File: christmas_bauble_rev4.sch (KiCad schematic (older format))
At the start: 23 parts

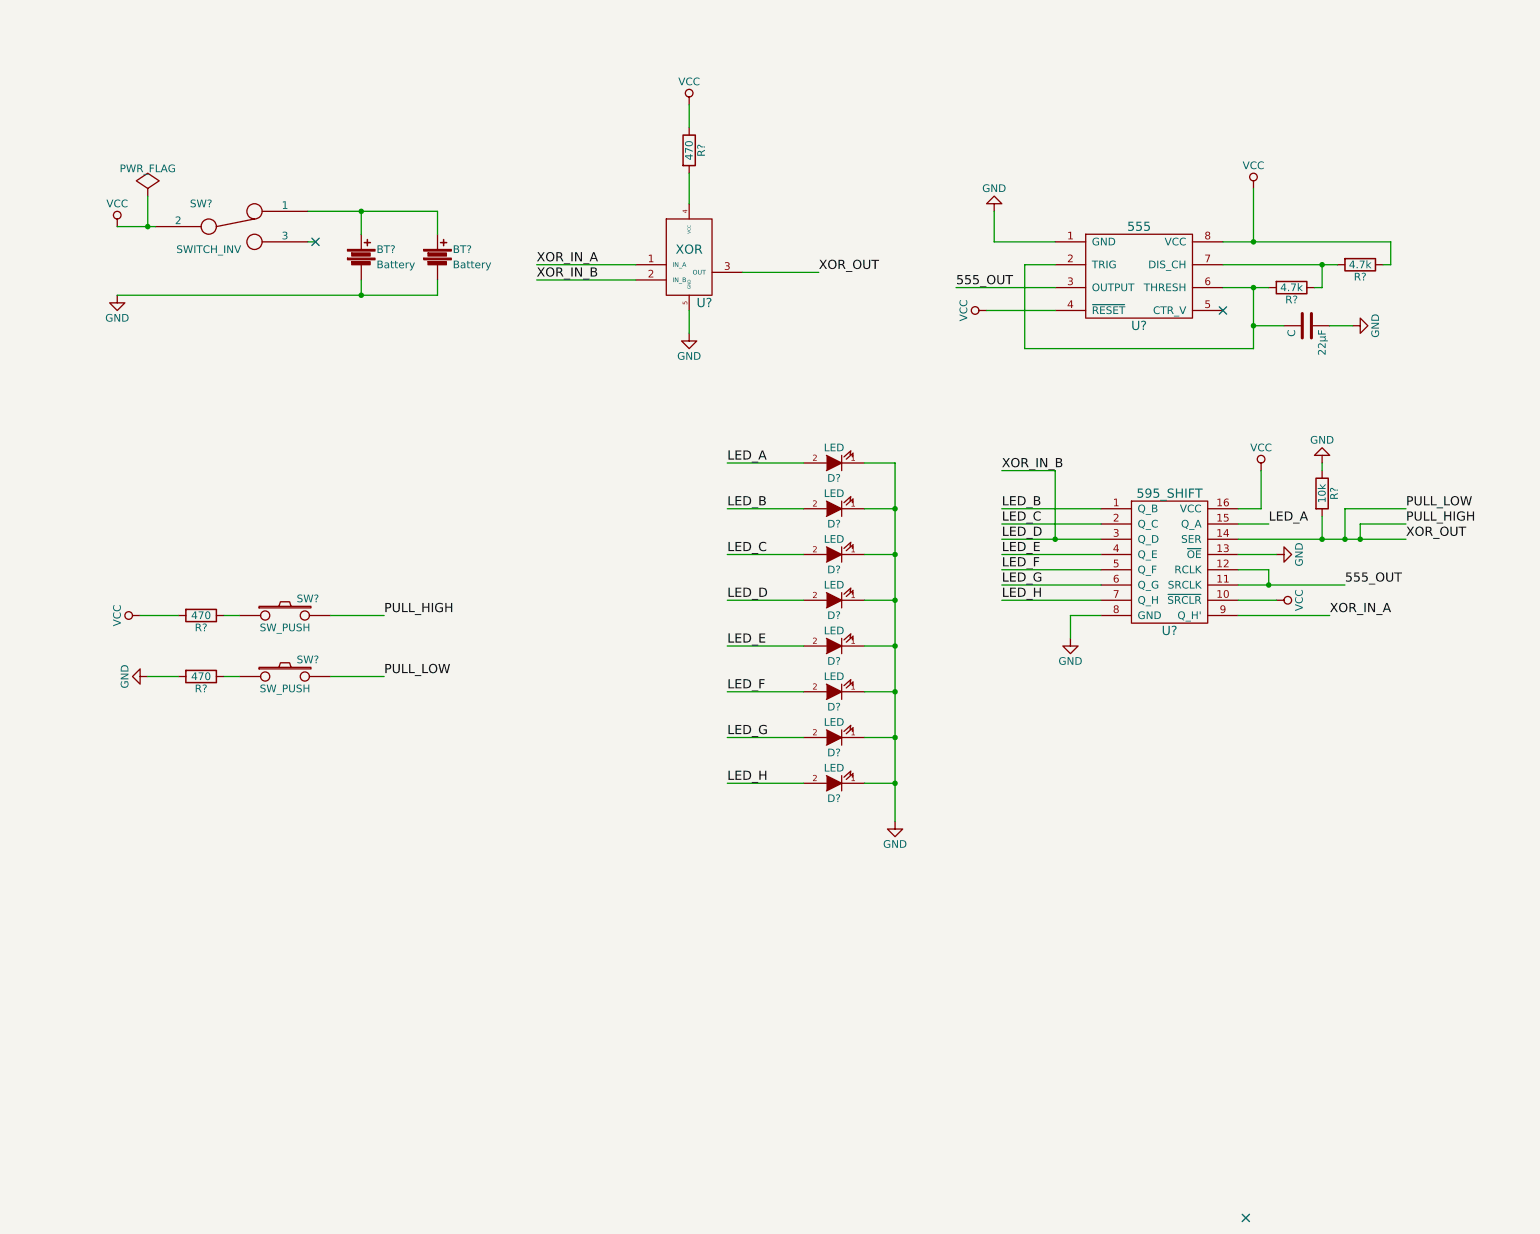
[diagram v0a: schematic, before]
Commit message: Adding dip switches to the layout to program the bauble
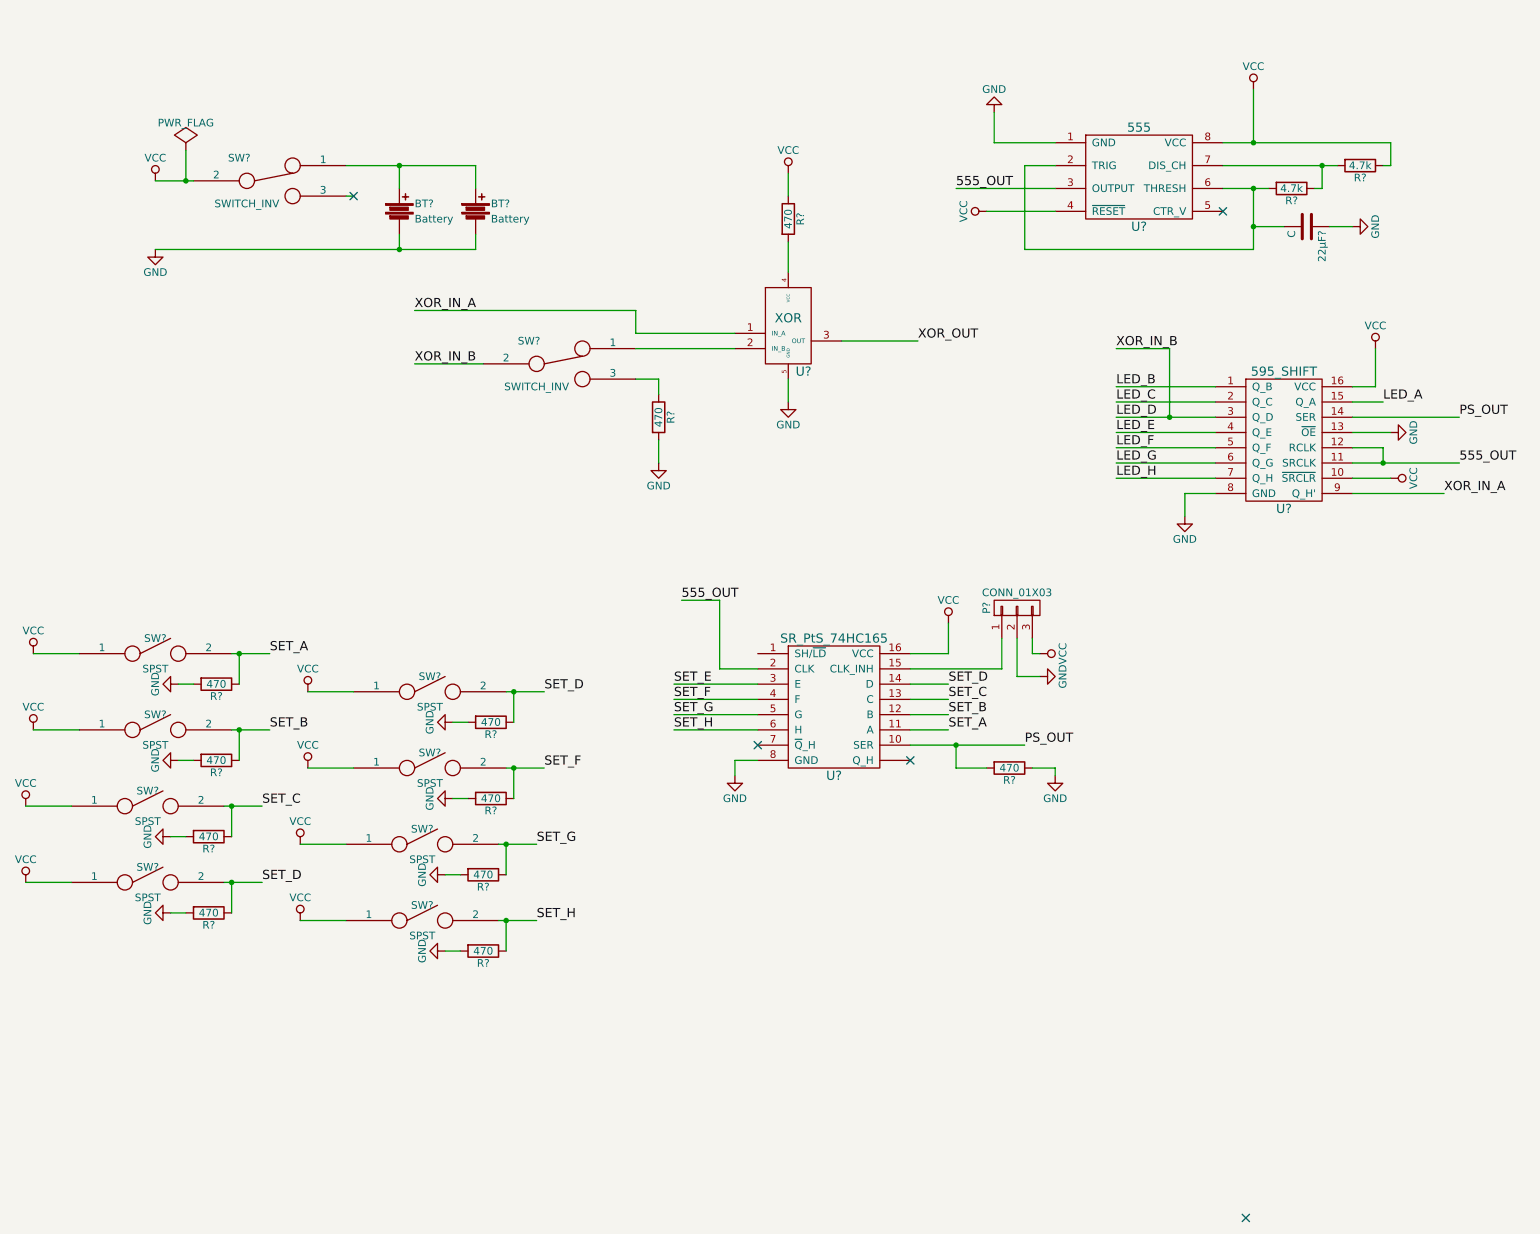
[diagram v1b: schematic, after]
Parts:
- removed D? (x8): LED, symbol LED
- removed R?: 10k, symbol R
- removed R? (x2): 470, symbol R
- removed SW? (x2): SW_PUSH, symbol SW_PUSH
- added P?: CONN_01X03, symbol CONN_01X03
- added R? (x10): 470, symbol R
- added SW? (x8): SPST, symbol SPST
- added SW?: SWITCH_INV, symbol SWITCH_INV
- added U?: SR_PtS_74HC165, symbol SR_PtS_74HC165
- renumbered 22µF to 22µF?
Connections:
- net 555_OUT: now also U?.2 (CLK)
- net GND: now also P?.2 (P2), R?.1, R?.2, R?.2, R?.2, R?.2, R?.2, R?.2, R?.2, R?.2, R?.2, U?.8 (GND)
- net LED_D: now also SW?.2; no longer U?.2 (IN_B)
- net VCC: now also P?.3 (P3), SW?.1, SW?.1, SW?.1, SW?.1, SW?.1, SW?.1, SW?.1, SW?.1, U?.16 (VCC)
- net PULL_HIGH renamed PS_OUT
- net PS_OUT: now also R?.2, U?.10 (SER); no longer U?.3 (OUT)
- new net: SW?.1, U?.2 (IN_B)
- new net: P?.1 (P1), U?.15 (CLK_INH)
- new net: R?.1, SW?.3
- new net SET_A: R?.1, SW?.2, U?.11 (A)
- new net SET_B: R?.1, SW?.2, U?.12 (B)
- new net SET_C: R?.1, SW?.2, U?.13 (C)
- new net SET_D: R?.1, R?.1, SW?.2, SW?.2, U?.14 (D)
- new net SET_E: U?.3 (E)
- new net SET_F: R?.1, SW?.2, U?.4 (F)
- new net SET_G: R?.1, SW?.2, U?.5 (G)
- new net SET_H: R?.1, SW?.2, U?.6 (H)
- new net XOR_OUT: U?.3 (OUT)
- no-connect marks 3 -> 5
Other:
- moved on the sheet: 22µF?, BT?, R?, SW?, U?

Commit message: Adding more debugging LEDs and a switch for 'Programmer mode'
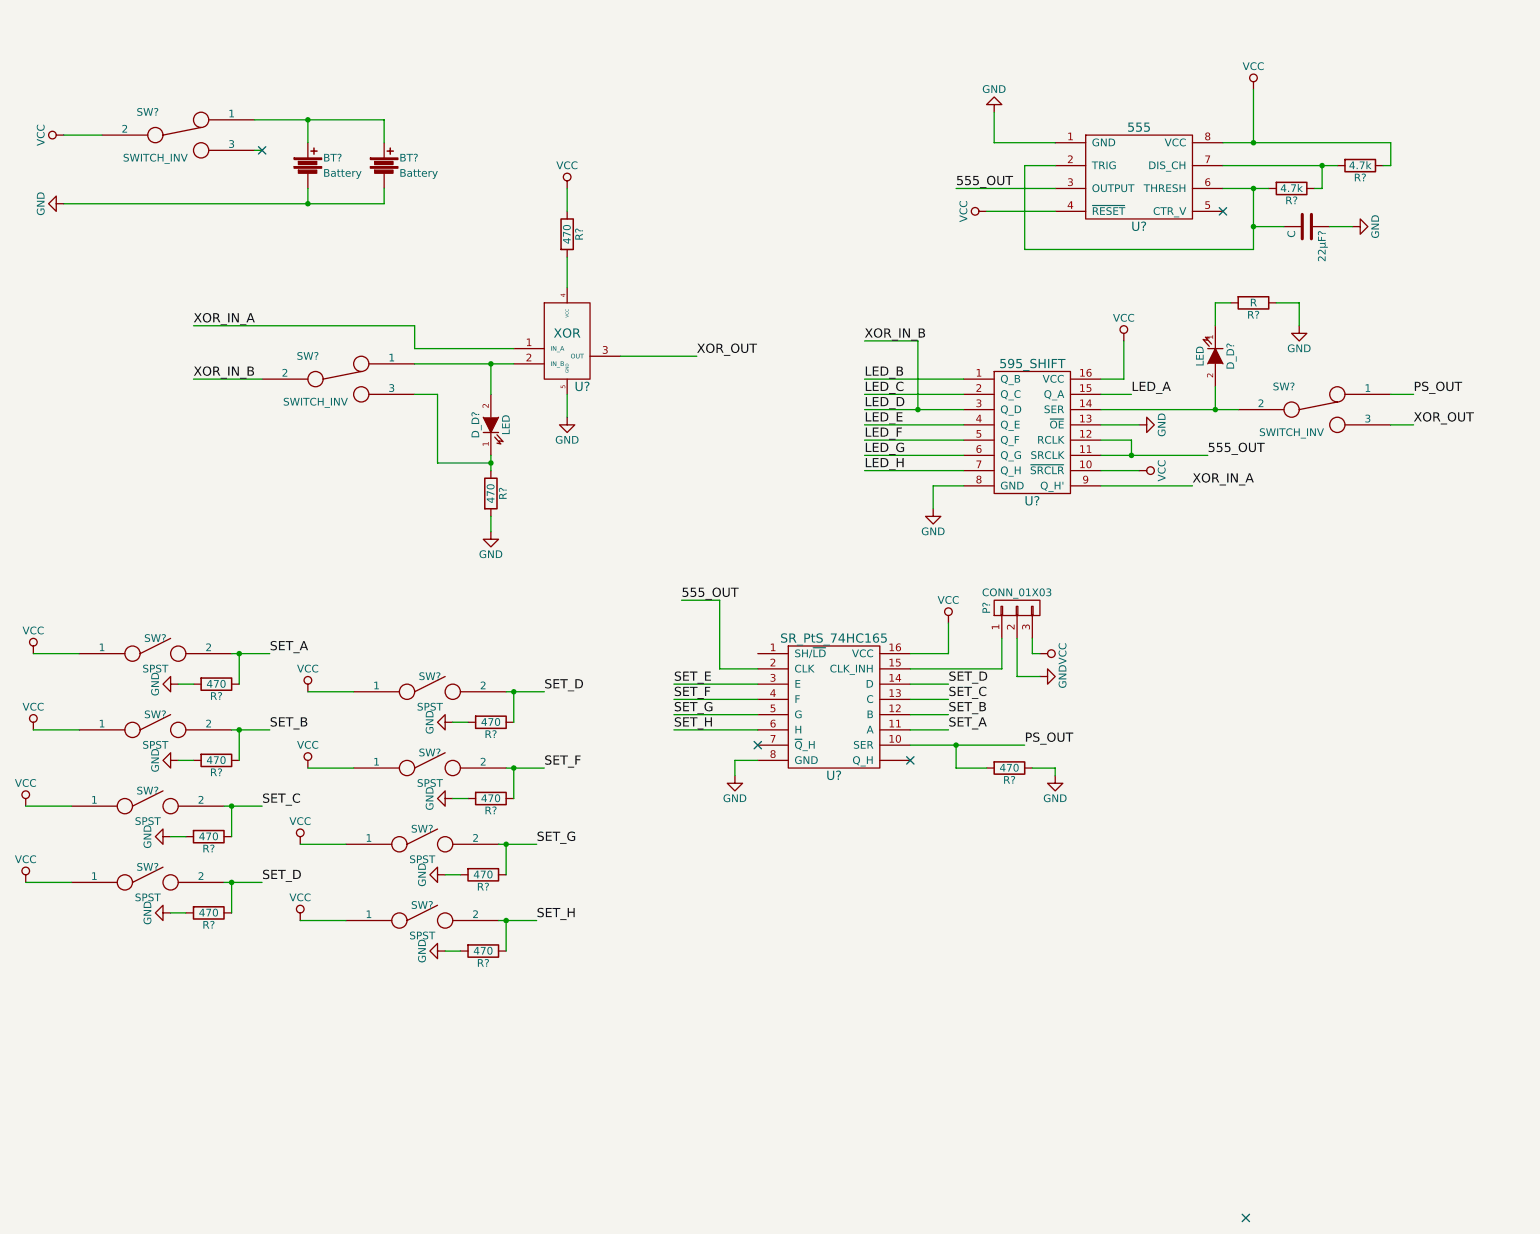
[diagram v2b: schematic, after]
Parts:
- removed R?: 470, symbol R
- added D_D? (x2): LED, symbol LED
- added R?: 470, symbol R
- added R?: R, symbol R
- added SW?: SWITCH_INV, symbol SWITCH_INV
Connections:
- net GND: now also R?.1, R?.2
- net PS_OUT: now also SW?.1; no longer U?.14 (SER)
- net XOR_OUT: now also SW?.3
- net at SW?.1, U?.2 (IN_B): now also D_D?.2 (A)
- net at SW?.3: now also D_D?.1 (K), R?.1
- new net: D_D?.2 (A), SW?.2, U?.14 (SER)
- new net: D_D?.1 (K), R?.2
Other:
- moved on the sheet: BT?, R?, SW?, U?

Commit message: Updating some revision 4 files.
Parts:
- removed D_D? (x2): LED, symbol LED
- removed R?: 4.7k, symbol R
- removed R? (x2): 470, symbol R
- removed R?: R, symbol R
- added D?: D, symbol D
- added P? (x2): CONN_01X03, symbol CONN_01X03
- added VR?: VR, symbol VR
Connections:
- net GND: now also P?.1 (P1), P?.3 (P3)
- net PS_OUT: now also U?.~ (Q_H); no longer U?.10 (SER)
- net VCC: now also P?.1 (P1), P?.3 (P3), VR?.1
- net at 22µF?.2, R?.2, U?.2 (TRIG)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: now also D?.1 (K)
- net at R?.1, U?.7 (DIS_CH): now also D?.2 (A), VR?.2
- net at U?.1 (SH/~LD): now also P?.2 (P2)
- new net: P?.2 (P2), U?.10 (SER)
- no-connect marks 5 -> 7
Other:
- note added: "Test Freq"
- moved on the sheet: 22µF?
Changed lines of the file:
@@
 Sheet 1 1
 Title "Christmas Bauble"
-Date "2016-01-01"
-Rev "Rev 4"
+Date "2016-02-13"
+Rev "Rev B"
 Comp ""
 Comment1 "Revision that gets put into production for soldering kits"
@@
 $EndComp
 $Comp
-L R R?
-U 1 1 5685F423
-P 9450 1500
-F 0 "R?" V 9530 1500 50  0000 C CNN
-F 1 "4.7k" V 9450 1500 50  0000 C CNN
-F 2 "" V 9380 1500 30  0000 C CNN
-F 3 "" H 9450 1500 30  0000 C CNN
-	1    9450 1500
-	0    1    1    0
-$EndComp
-$Comp
 L VCC #PWR?
 U 1 1 5685F6A7
@@
 L C 22µF?
 U 1 1 56860DDF
-P 9100 1900
-F 0 "22µF?" H 9125 2000 50  0000 L CNN
-F 1 "C" H 9125 1800 50  0000 L CNN
-F 2 "" H 9138 1750 30  0000 C CNN
-F 3 "" H 9100 1900 60  0000 C CNN
-	1    9100 1900
+P 9100 2350
+F 0 "22µF?" H 9125 2450 50  0000 L CNN
+F 1 "C" H 9125 2250 50  0000 L CNN
+F 2 "" H 9138 2200 30  0000 C CNN
+F 3 "" H 9100 2350 60  0000 C CNN
+	1    9100 2350
 	0    1    1    0
 $EndComp
@@
 L GND #PWR?
 U 1 1 56860ED4
-P 9400 1900
-F 0 "#PWR?" H 9400 1650 50  0001 C CNN
-F 1 "GND" H 9400 1750 50  0000 C CNN
-F 2 "" H 9400 1900 60  0000 C CNN
-F 3 "" H 9400 1900 60  0000 C CNN
-	1    9400 1900
+P 9400 2350
+F 0 "#PWR?" H 9400 2100 50  0001 C CNN
+F 1 "GND" H 9400 2200 50  0000 C CNN
+F 2 "" H 9400 2350 60  0000 C CNN
+F 3 "" H 9400 2350 60  0000 C CNN
+	1    9400 2350
 	0    -1   -1   0
 $EndComp
@@
 	1    0    0    -1
 $EndComp
-Text Label 5000 4350 0    60   ~ 0
+Text Label 4550 4350 0    60   ~ 0
 555_OUT
-Text Label 7250 5300 0    60   ~ 0
+Text Label 6750 5400 0    60   ~ 0
 PS_OUT
-NoConn ~ 6500 5400
 NoConn ~ 5500 5300
 $Comp
@@
 PS_OUT
 $Comp
-L R R?
-U 1 1 568DB16E
-P 7150 5450
-F 0 "R?" V 7230 5450 50  0000 C CNN
-F 1 "470" V 7150 5450 50  0000 C CNN
-F 2 "" V 7080 5450 30  0000 C CNN
-F 3 "" H 7150 5450 30  0000 C CNN
-	1    7150 5450
-	0    1    1    0
-$EndComp
-$Comp
 L GND #PWR?
 U 1 1 568DB280
-P 7450 5500
-F 0 "#PWR?" H 7450 5250 50  0001 C CNN
-F 1 "GND" H 7450 5350 50  0000 C CNN
-F 2 "" H 7450 5500 60  0000 C CNN
-F 3 "" H 7450 5500 60  0000 C CNN
-	1    7450 5500
+P 7850 5350
+F 0 "#PWR?" H 7850 5100 50  0001 C CNN
+F 1 "GND" H 7850 5200 50  0000 C CNN
+F 2 "" H 7850 5350 60  0000 C CNN
+F 3 "" H 7850 5350 60  0000 C CNN
+	1    7850 5350
 	1    0    0    -1
 $EndComp
@@
 $EndComp
 $Comp
-L LED D_D?
-U 1 1 568DC6DF
-P 3750 3200
-F 0 "D_D?" H 3750 3300 50  0000 C CNN
-F 1 "LED" H 3750 3100 50  0000 C CNN
-F 2 "" H 3750 3200 60  0000 C CNN
-F 3 "" H 3750 3200 60  0000 C CNN
-	1    3750 3200
-	0    -1   -1   0
-$EndComp
-$Comp
-L R R?
-U 1 1 568DC944
-P 3750 3650
-F 0 "R?" V 3830 3650 50  0000 C CNN
-F 1 "470" V 3750 3650 50  0000 C CNN
-F 2 "" V 3680 3650 30  0000 C CNN
-F 3 "" H 3750 3650 30  0000 C CNN
-	1    3750 3650
-	1    0    0    -1
-$EndComp
-$Comp
-L GND #PWR?
-U 1 1 568DCA56
-P 3750 3900
-F 0 "#PWR?" H 3750 3650 50  0001 C CNN
-F 1 "GND" H 3750 3750 50  0000 C CNN
-F 2 "" H 3750 3900 60  0000 C CNN
-F 3 "" H 3750 3900 60  0000 C CNN
-	1    3750 3900
-	1    0    0    -1
-$EndComp
-$Comp
 L SWITCH_INV SW?
 U 1 1 568DD1E4
@@
 Connection ~ 6550 3100
 Wire Wire Line
-	8750 1650 8750 2050
-Wire Wire Line
-	8750 2050 7250 2050
-Wire Wire Line
-	7250 2050 7250 1500
+	8750 1650 8750 2350
+Wire Wire Line
+	7250 2000 8850 2000
+Wire Wire Line
+	7250 2000 7250 1500
 Wire Wire Line
 	7250 1500 7450 1500
@@
 	8550 1650 8850 1650
 Wire Wire Line
-	8550 1500 9300 1500
+	8550 1500 9400 1500
 Wire Wire Line
 	9150 1650 9200 1650
 Wire Wire Line
-	9200 1650 9200 1500
+	9200 1500 9200 2000
 Connection ~ 9200 1500
 Wire Wire Line
-	9600 1500 9650 1500
-Wire Wire Line
-	9650 1500 9650 1350
-Wire Wire Line
-	9650 1350 8550 1350
+	9950 1350 9950 1500
+Wire Wire Line
+	8550 1350 9950 1350
 Wire Wire Line
 	8750 1350 8750 1000
@@
 	7450 1800 7000 1800
 Wire Wire Line
-	7450 1650 6800 1650
-Wire Wire Line
-	8750 1900 8950 1900
-Connection ~ 8750 1900
-Wire Wire Line
-	9250 1900 9400 1900
+	6800 1650 7450 1650
+Wire Wire Line
+	9250 2350 9400 2350
 Wire Wire Line
 	3900 2700 3250 2700
@@
 	5350 5400 5350 5500
 Wire Wire Line
-	5250 4350 5250 4800
-Wire Wire Line
-	5250 4800 5500 4800
-Wire Wire Line
-	5250 4350 5000 4350
-Wire Wire Line
-	6500 5300 7250 5300
+	4950 4800 5500 4800
+Wire Wire Line
+	4550 4350 4950 4350
 Wire Wire Line
 	1800 2900 2250 2900
@@
 	3250 3000 3400 3000
 Wire Wire Line
-	3400 3000 3400 3450
-Wire Wire Line
 	1800 2550 3250 2550
 Wire Wire Line
 	3250 2550 3250 2700
 Wire Wire Line
-	6800 5300 6800 5450
-Wire Wire Line
-	6800 5450 7000 5450
-Connection ~ 6800 5300
-Wire Wire Line
-	7300 5450 7450 5450
-Wire Wire Line
-	7450 5450 7450 5500
+	7500 5300 7850 5300
+Wire Wire Line
+	7850 5300 7850 5350
 Wire Wire Line
 	6500 4800 7100 4800
@@
 Connection ~ 3750 2800
 Wire Wire Line
-	3750 3400 3750 3500
-Wire Wire Line
-	3750 3800 3750 3900
-Wire Wire Line
-	3400 3450 3750 3450
-Connection ~ 3750 3450
-Wire Wire Line
 	9800 3000 9650 3000
 Wire Wire Line
@@
 Wire Wire Line
 	7750 3100 8650 3100
-$Comp
-L LED D_D?
-U 1 1 568DE83B
-P 8500 2750
-F 0 "D_D?" H 8500 2850 50  0000 C CNN
-F 1 "LED" H 8500 2650 50  0000 C CNN
-F 2 "" H 8500 2750 60  0000 C CNN
-F 3 "" H 8500 2750 60  0000 C CNN
-	1    8500 2750
-	0    1    1    0
-$EndComp
-Wire Wire Line
-	8500 2950 8500 3100
+Wire Wire Line
+	7350 1650 7350 650
+Wire Wire Line
+	7350 650  7950 650
+Connection ~ 7350 1650
+Text Notes 7850 600  0    60   ~ 0
+Test Freq
+$Comp
+L VR VR?
+U 1 1 568D51BE
+P 9650 1500
+F 0 "VR?" V 9710 1454 50  0000 C TNN
+F 1 "VR" V 9650 1500 50  0000 C CNN
+F 2 "" H 9650 1500 60  0000 C CNN
+F 3 "" H 9650 1500 60  0000 C CNN
+	1    9650 1500
+	0    1    1    0
+$EndComp
+Wire Wire Line
+	9950 1500 9900 1500
+NoConn ~ 7950 650
+Wire Wire Line
+	8500 3100 8500 2750
 Connection ~ 8500 3100
-$Comp
-L R R?
-U 1 1 568DE99C
-P 8750 2400
-F 0 "R?" V 8830 2400 50  0000 C CNN
-F 1 "R" V 8750 2400 50  0000 C CNN
-F 2 "" V 8680 2400 30  0000 C CNN
-F 3 "" H 8750 2400 30  0000 C CNN
-	1    8750 2400
-	0    1    1    0
-$EndComp
-Wire Wire Line
-	8600 2400 8500 2400
-Wire Wire Line
-	8500 2400 8500 2550
-Wire Wire Line
-	8900 2400 9050 2400
-Wire Wire Line
-	9050 2400 9050 2550
-$Comp
-L GND #PWR?
-U 1 1 568DEC1F
-P 9050 2550
-F 0 "#PWR?" H 9050 2300 50  0001 C CNN
-F 1 "GND" H 9050 2400 50  0000 C CNN
-F 2 "" H 9050 2550 60  0000 C CNN
-F 3 "" H 9050 2550 60  0000 C CNN
-	1    9050 2550
-	1    0    0    -1
-$EndComp
+NoConn ~ 8500 2750
+$Comp
+L D D?
+U 1 1 569068DC
+P 9000 2000
+F 0 "D?" H 9000 2100 50  0000 C CNN
+F 1 "D" H 9000 1900 50  0000 C CNN
+F 2 "" H 9000 2000 60  0000 C CNN
+F 3 "" H 9000 2000 60  0000 C CNN
+	1    9000 2000
+	1    0    0    -1
+$EndComp
+Connection ~ 8750 2000
+Wire Wire Line
+	9200 2000 9150 2000
+Connection ~ 9200 1650
+Wire Wire Line
+	8750 2350 8950 2350
+Wire Wire Line
+	6500 5400 6750 5400
+Wire Wire Line
+	6500 5300 7400 5300
+$Comp
+L CONN_01X03 P?
+U 1 1 56919F26
+P 7400 5600
+F 0 "P?" H 7400 5800 50  0000 C CNN
+F 1 "CONN_01X03" V 7500 5600 50  0000 C CNN
+F 2 "" H 7400 5600 60  0000 C CNN
+F 3 "" H 7400 5600 60  0000 C CNN
+	1    7400 5600
+	0    1    1    0
+$EndComp
+Wire Wire Line
+	7400 5300 7400 5400
+Wire Wire Line
+	7500 5300 7500 5400
+$Comp
+L VCC #PWR?
+U 1 1 5691A21E
+P 7300 5200
+F 0 "#PWR?" H 7300 5050 50  0001 C CNN
+F 1 "VCC" H 7300 5350 50  0000 C CNN
+F 2 "" H 7300 5200 60  0000 C CNN
+F 3 "" H 7300 5200 60  0000 C CNN
+	1    7300 5200
+	1    0    0    -1
+$EndComp
+Wire Wire Line
+	7300 5200 7300 5400
+Wire Wire Line
+	4950 4350 4950 4800
+$Comp
+L CONN_01X03 P?
+U 1 1 5691B096
+P 5350 4100
+F 0 "P?" H 5350 4300 50  0000 C CNN
+F 1 "CONN_01X03" V 5450 4100 50  0000 C CNN
+F 2 "" H 5350 4100 60  0000 C CNN
+F 3 "" H 5350 4100 60  0000 C CNN
+	1    5350 4100
+	0    -1   -1   0
+$EndComp
+Wire Wire Line
+	5500 4700 5350 4700
+Wire Wire Line
+	5350 4700 5350 4300
+$Comp
+L VCC #PWR?
+U 1 1 5691B1EE
+P 5250 4350
+F 0 "#PWR?" H 5250 4200 50  0001 C CNN
+F 1 "VCC" H 5250 4500 50  0000 C CNN
+F 2 "" H 5250 4350 60  0000 C CNN
+F 3 "" H 5250 4350 60  0000 C CNN
+	1    5250 4350
+	-1   0    0    1
+$EndComp
+Wire Wire Line
+	5250 4350 5250 4300
+$Comp
+L GND #PWR?
+U 1 1 5691B304
+P 5450 4350
+F 0 "#PWR?" H 5450 4100 50  0001 C CNN
+F 1 "GND" H 5450 4200 50  0000 C CNN
+F 2 "" H 5450 4350 60  0000 C CNN
+F 3 "" H 5450 4350 60  0000 C CNN
+	1    5450 4350
+	1    0    0    -1
+$EndComp
+Wire Wire Line
+	5450 4300 5450 4350
+NoConn ~ 3750 3000
 $EndSCHEMATC
